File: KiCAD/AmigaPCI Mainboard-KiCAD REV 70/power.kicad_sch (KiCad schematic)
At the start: 85 parts, among them CN205 Case Fan, CN210 _KBRST, CN601 ATX-24, J11 _REGEN, Q202 AO3400A, U200 74LVC2G34, U206 MIC1232, U215 74HC03, U219 74AHC04, U220 74LVC08, U222 74HCT4066, U229 74CBT16233, U231 74LVC08, U232 74AHC1G09, U303 74HCT74, U600 AP2114H-3.3, U601 AP2114H-1.2, U602 LM79L05

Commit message: Add JLCPCB part numbers and fix 74LVC244 footprints.
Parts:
- C110, C111, C112, C113, C114, C115, C116, C117, C118, C119, C120, C121, C133, C134, C601: LCSC (none) -> C141282
- C200, C201, C223, C251, C263, C615, C616: LCSC (none) -> C14663
- C600, C602, C603, C604, C605, C606, C607, C609, C610, C614, C620, C621, C622, C624: LCSC (none) -> C88724
- C608, C611, C613, C619, C625: LCSC (none) -> C88726
- C617, C618, C623, C626: LCSC (none) -> C19666
- CN205: LCSC (none) -> C240840
- CN210: LCSC (none) -> C42419937
- CN601: LCSC (none) -> C114088
- CN_CASE1: LCSC (none) -> C7430400
- D204: LCSC (none) -> C118873
- D205: LCSC (none) -> C2117
- J11: LCSC (none) -> C81276
- Q202: LCSC (none) -> C347475
- R227, R250, R254: LCSC (none) -> C21190
- R228, R241, R279: LCSC (none) -> C25804
- R247: LCSC (none) -> C8218
- U200: LCSC (none) -> C14461
- U206: LCSC (none) -> C627729
- U215: LCSC (none) -> C546492
- U219: LCSC (none) -> C8190
- U220, U231: LCSC (none) -> C6053
- U222: LCSC (none) -> C26433
- U229: LCSC (none) -> C2674759
- U232: LCSC (none) -> C840099
- U303: LCSC (none) -> C141335
- U600: LCSC (none) -> C150716
- U601: LCSC (none) -> C94854
- U602: LCSC (none) -> C7555

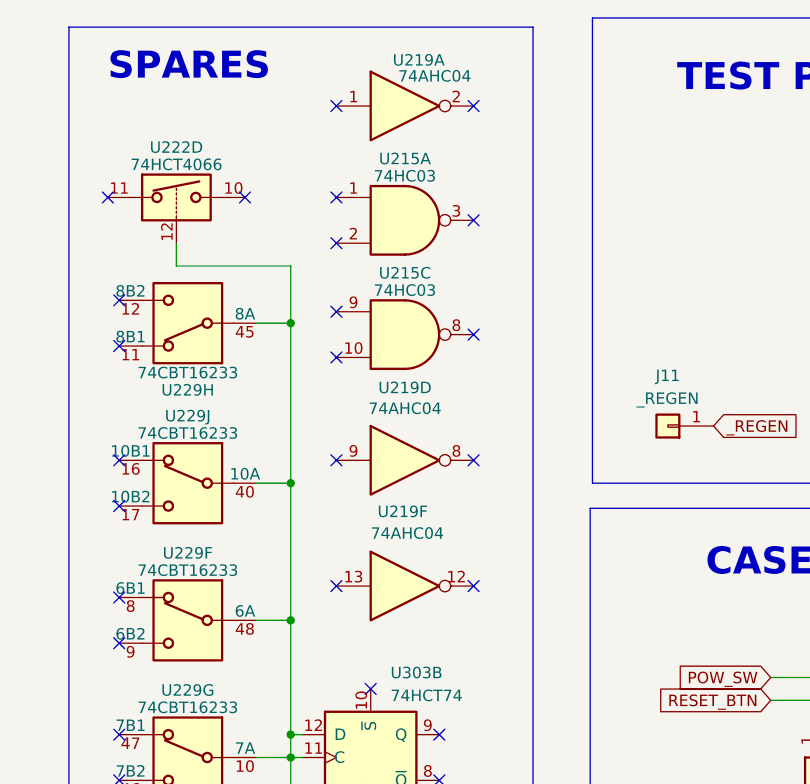
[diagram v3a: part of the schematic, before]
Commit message: Updates to revision 7 board.
Change U810 to 74LVC245 buffers
Add CDAC to U712
Add address latch to CIAs
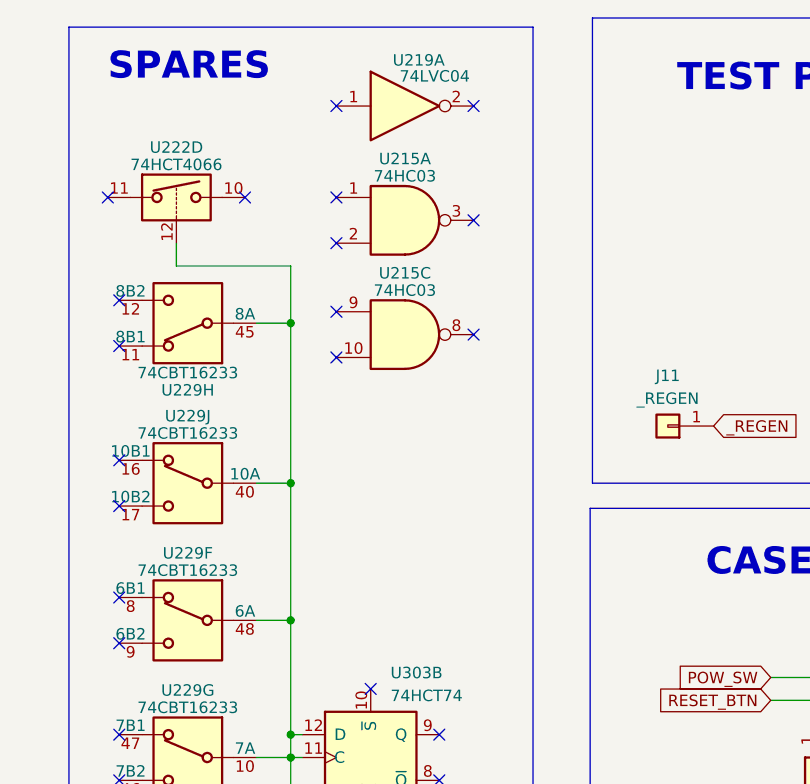
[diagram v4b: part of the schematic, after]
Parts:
- removed unit 6 of U219
- removed unit 4 of U219
- U219: value 74AHC04 -> 74LVC04; LCSC C8190 -> C352968
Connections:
- no-connect marks 28 -> 24
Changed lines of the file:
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@@
 	(title_block
 		(title "AMIGA PCI")
-		(date "2026-04-27")
+		(date "2026-06-06")
 		(rev "7.0")
 	)
@@
 	)
 	(no_connect
-		(at 290.83 67.31)
-	)
-	(no_connect
 		(at 290.83 43.18)
 	)
 	(no_connect
-		(at 290.83 81.28)
-	)
-	(no_connect
 		(at 290.83 50.8)
 	)
@@
 	)
 	(no_connect
-		(at 306.07 81.28)
-	)
-	(no_connect
 		(at 76.2 185.42)
 	)
@@
 	)
 	(no_connect
-		(at 306.07 67.31)
-	)
-	(no_connect
 		(at 265.43 38.1)
 	)
@@
 	)
 	(symbol
-		(lib_id "74xx:74LS04")
-		(at 298.45 81.28 0)
-		(unit 6)
-		(exclude_from_sim no)
-		(in_bom yes)
-		(on_board yes)
-		(dnp no)
-		(property "Reference" "U219"
-			(at 298.196 73.025 0)
-			(effects
-				(font
-					(size 1.27 1.27)
-				)
-			)
-		)
-		(property "Value" "74AHC04"
-			(at 298.704 75.438 0)
-			(effects
-				(font
-					(size 1.27 1.27)
-				)
-			)
-		)
-		(property "Footprint" "Package_SO:TSSOP-14_4.4x5mm_P0.65mm"
-			(at 298.45 81.28 0)
-			(effects
-				(font
-					(size 1.27 1.27)
-				)
-				(hide yes)
-			)
-		)
-		(property "Datasheet" "http://www.ti.com/lit/gpn/sn74LS04"
-			(at 298.45 81.28 0)
-			(effects
-				(font
-					(size 1.27 1.27)
-				)
-				(hide yes)
-			)
-		)
-		(property "Description" ""
-			(at 298.45 81.28 0)
-			(effects
-				(font
-					(size 1.27 1.27)
-				)
-				(hide yes)
-			)
-		)
-		(property "LCSC" "C8190"
-			(at 298.45 81.28 0)
-			(effects
-				(font
-					(size 1.27 1.27)
-				)
-				(hide yes)
-			)
-		)
-		(pin "1"
-		)
-		(pin "2"
-		)
-		(pin "3"
-		)
-		(pin "4"
-		)
-		(pin "5"
-		)
-		(pin "6"
-		)
-		(pin "8"
-		)
-		(pin "9"
-		)
-		(pin "10"
-		)
-		(pin "11"
-		)
-		(pin "12"
-		)
-		(pin "13"
-		)
-		(pin "14"
-		)
-		(pin "7"
-		)
-		(instances
-			(project "AmigaPCI Mainboard"
-				(path "/72453515-27fe-4336-91f3-e3c8054f7767/4cb777ef-2899-49f4-b38f-a0c07d84fa7d"
-					(reference "U219")
-					(unit 6)
-				)
-			)
-		)
-	)
-	(symbol
 		(lib_name "GND_1")
 		(lib_id "power:GND")
@@
 	)
 	(symbol
-		(lib_id "74xx:74LS04")
-		(at 298.45 67.31 0)
-		(unit 4)
-		(exclude_from_sim no)
-		(in_bom yes)
-		(on_board yes)
-		(dnp no)
-		(property "Reference" "U219"
-			(at 298.45 59.2582 0)
-			(effects
-				(font
-					(size 1.27 1.27)
-				)
-			)
-		)
-		(property "Value" "74AHC04"
-			(at 298.45 61.5696 0)
-			(effects
-				(font
-					(size 1.27 1.27)
-				)
-			)
-		)
-		(property "Footprint" "Package_SO:TSSOP-14_4.4x5mm_P0.65mm"
-			(at 298.45 67.31 0)
-			(effects
-				(font
-					(size 1.27 1.27)
-				)
-				(hide yes)
-			)
-		)
-		(property "Datasheet" "http://www.ti.com/lit/gpn/sn74LS04"
-			(at 298.45 67.31 0)
-			(effects
-				(font
-					(size 1.27 1.27)
-				)
-				(hide yes)
-			)
-		)
-		(property "Description" ""
-			(at 298.45 67.31 0)
-			(effects
-				(font
-					(size 1.27 1.27)
-				)
-				(hide yes)
-			)
-		)
-		(property "LCSC" "C8190"
-			(at 298.45 67.31 0)
-			(effects
-				(font
-					(size 1.27 1.27)
-				)
-				(hide yes)
-			)
-		)
-		(pin "1"
-		)
-		(pin "2"
-		)
-		(pin "3"
-		)
-		(pin "4"
-		)
-		(pin "5"
-		)
-		(pin "6"
-		)
-		(pin "8"
-		)
-		(pin "9"
-		)
-		(pin "10"
-		)
-		(pin "11"
-		)
-		(pin "12"
-		)
-		(pin "13"
-		)
-		(pin "14"
-		)
-		(pin "7"
-		)
-		(instances
-			(project "AmigaPCI Mainboard"
-				(path "/72453515-27fe-4336-91f3-e3c8054f7767/4cb777ef-2899-49f4-b38f-a0c07d84fa7d"
-					(reference "U219")
-					(unit 4)
-				)
-			)
-		)
-	)
-	(symbol
 		(lib_id "power:-12V")
 		(at 222.25 33.02 0)
@@
 			)
 		)
-		(property "Value" "74AHC04"
+		(property "Value" "74LVC04"
 			(at 301.752 24.638 0)
 			(effects
@@
 			)
 		)
-		(property "LCSC" "C8190"
+		(property "LCSC" " C352968"
 			(at 298.45 27.94 0)
 			(effects

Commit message: New hardware rev files.
Gerber
BOM w/JLCPCB part numbers
Pick-n-Place File
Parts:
- C110, C111, C112, C113, C114, C115, C116, C117, C118, C119, C120, C121, C133, C134, C601: LCSC C141282 -> C106643
- U215: LCSC C546492 -> C2869660
- U219: LCSC C352968 -> C352968
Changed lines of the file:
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@@
 			)
 		)
-		(property "LCSC" "C141282"
+		(property "LCSC" "C106643"
 			(at 325.12 156.21 0)
 			(effects
@@
 			)
 		)
-		(property "LCSC" "C141282"
+		(property "LCSC" "C106643"
 			(at 405.13 156.21 0)
 			(effects
@@
 			)
 		)
-		(property "LCSC" "C141282"
+		(property "LCSC" "C106643"
 			(at 351.79 156.21 0)
 			(effects
@@
 			)
 		)
-		(property "LCSC" "C141282"
+		(property "LCSC" "C106643"
 			(at 378.46 156.21 0)
 			(effects
@@
 			)
 		)
-		(property "LCSC" "C141282"
+		(property "LCSC" "C106643"
 			(at 284.48 156.21 0)
 			(effects
@@
 			)
 		)
-		(property "LCSC" "C141282"
+		(property "LCSC" "C106643"
 			(at 245.11 156.21 0)
 			(effects
@@
 			)
 		)
-		(property "LCSC" "C546492"
+		(property "LCSC" "C2869660"
 			(at 298.45 40.64 0)
 			(effects
@@
 			)
 		)
-		(property "LCSC" "C141282"
+		(property "LCSC" "C106643"
 			(at 364.49 156.21 0)
 			(effects
@@
 			)
 		)
-		(property "LCSC" " C352968"
+		(property "LCSC" "C352968"
 			(at 298.45 27.94 0)
 			(effects
@@
 			)
 		)
-		(property "LCSC" "C141282"
+		(property "LCSC" "C106643"
 			(at 298.45 156.21 0)
 			(effects
@@
 			)
 		)
-		(property "LCSC" "C141282"
+		(property "LCSC" "C106643"
 			(at 392.43 156.21 0)
 			(effects
@@
 			)
 		)
-		(property "LCSC" "C141282"
+		(property "LCSC" "C106643"
 			(at 228.6 156.21 0)
 			(effects
@@
 			)
 		)
-		(property "LCSC" "C141282"
+		(property "LCSC" "C106643"
 			(at 312.42 156.21 0)
 			(effects
@@
 			)
 		)
-		(property "LCSC" "C141282"
+		(property "LCSC" "C106643"
 			(at 337.82 156.21 0)
 			(effects
@@
 			)
 		)
-		(property "LCSC" "C546492"
+		(property "LCSC" "C2869660"
 			(at 298.45 53.34 0)
 			(effects
@@
 			)
 		)
-		(property "LCSC" "C141282"
+		(property "LCSC" "C106643"
 			(at 257.81 156.21 0)
 			(effects
@@
 			)
 		)
-		(property "LCSC" "C141282"
+		(property "LCSC" "C106643"
 			(at 130.81 46.99 0)
 			(effects
@@
 			)
 		)
-		(property "LCSC" "C141282"
+		(property "LCSC" "C106643"
 			(at 270.51 156.21 0)
 			(effects
